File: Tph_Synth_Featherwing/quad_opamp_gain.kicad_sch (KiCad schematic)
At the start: 26 parts, among them U3 Opamp_Quad_Generic

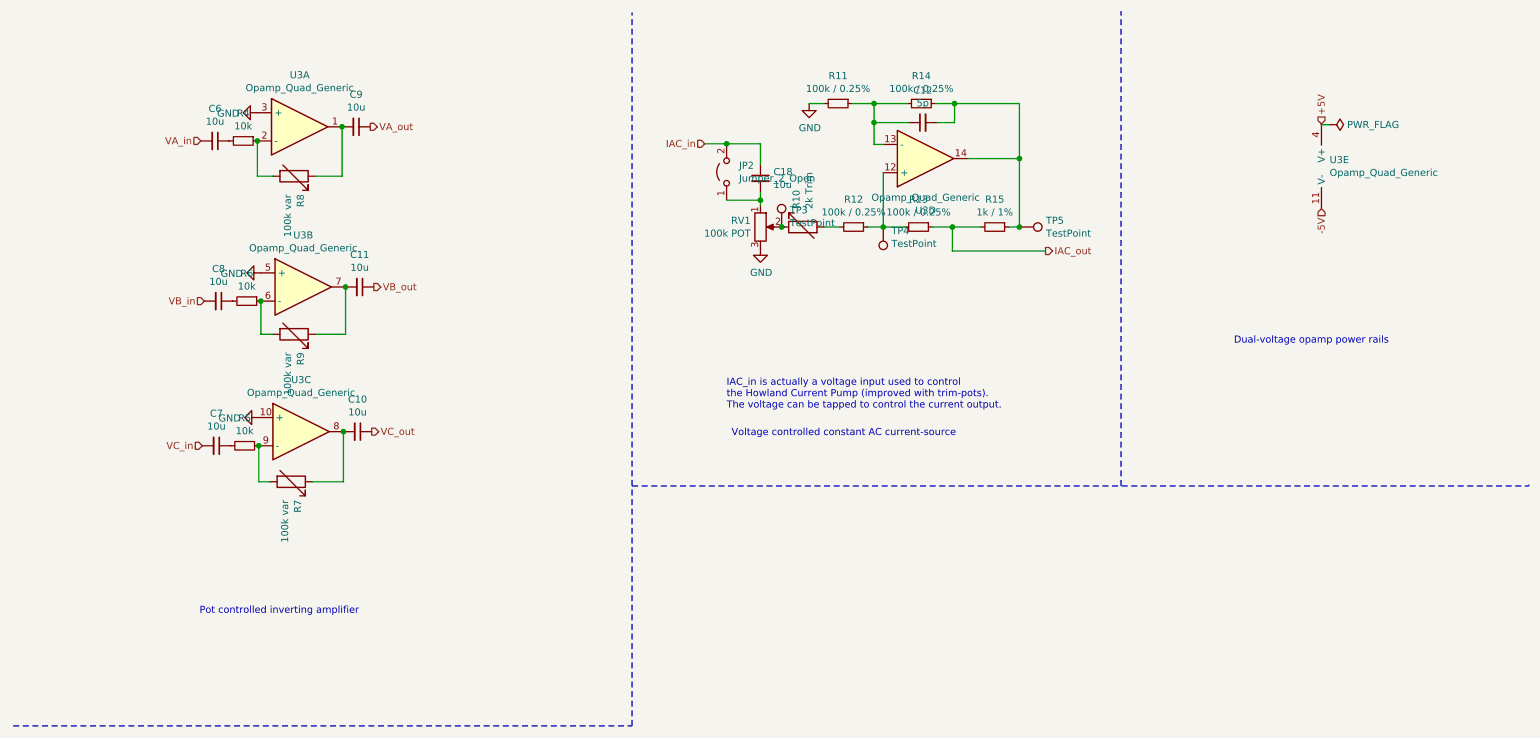
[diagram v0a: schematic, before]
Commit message: Upgrade design to KiCad 10; clear ERC and DRC violations
Co-authored-by: Copilot <223556219+Copilot@users.noreply.github.com>
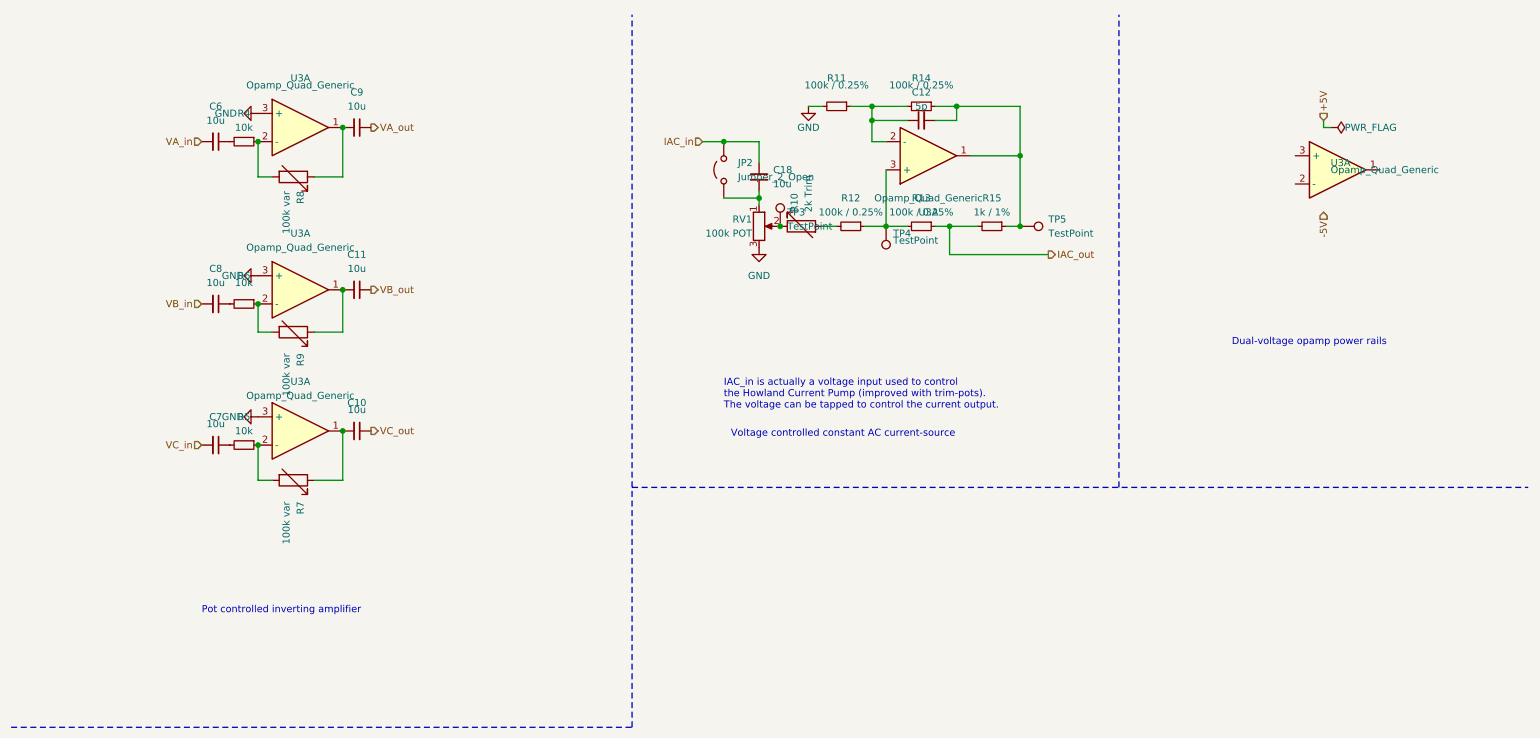
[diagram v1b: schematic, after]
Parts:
- RV1: symbol Device:R_POT -> Device:R_Potentiometer
- U3: symbol Device:Opamp_Quad_Generic -> Device:Opamp_Quad
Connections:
- net +5V: no longer U3.4 (V+)
- net -5V: no longer U3.11 (V-)
- net GND: now also U3.3 (+), U3.3 (+); no longer U3.10 (+), U3.5 (+)
- net at R6.1, R9.2: now also U3.2 (-); no longer U3.6 (-)
- net at C11.2, R9.1: now also U3.1; no longer U3.7
- net at C10.2, R7.1: now also U3.1; no longer U3.8
- net at R5.1, R7.2: now also U3.2 (-); no longer U3.9 (-)
- net at R12.1, R13.2, TP4.1: now also U3.3 (+); no longer U3.12 (+)
- net at C12.1, R11.1, R14.2: now also U3.2 (-); no longer U3.13 (-)
- net at C12.2, R14.1, R15.1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: now also U3.1; no longer U3.14
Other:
- moved on the sheet: C11, C8, R11, R12, R13, R14, R15, R6, TP4, U3A

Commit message: Release v0.4 with complete KiCad 10 schematic-PCB parity
Synchronize pad nets, schematic paths, component fields and BOM exclusions while retaining routing and placement. Restore project-local STEP models, fix edge silkscreen using local footprint variants, update revision metadata and improve schematic readability. Include inspected PDF and PCB renders.

Co-authored-by: Copilot <223556219+Copilot@users.noreply.github.com>
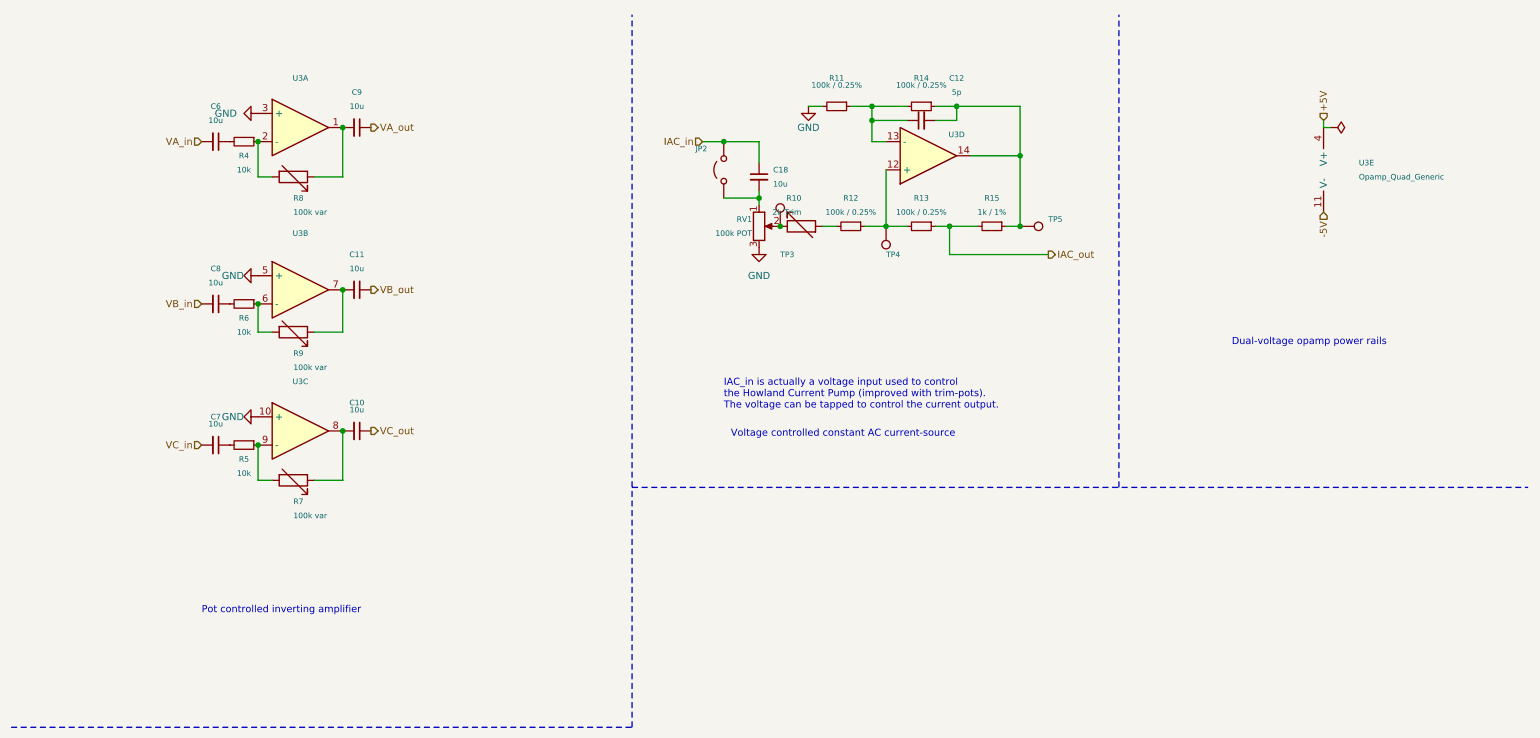
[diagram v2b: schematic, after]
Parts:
- JP2, TP3, TP4, TP5: now left out of the parts list
- R7, R8, R9, RV1: footprint Potentiometer_THT:Potentiometer_Bourns_PTV09A-2_Single_Horizontal -> FeatherWing_v04:Potentiometer_Bourns_PTV09A-2_Single_Horizontal_EdgeMounted
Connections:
- net +5V: now also U3.4 (V+)
- net -5V: now also U3.11 (V-)
- net GND: now also U3.10 (+), U3.5 (+); no longer U3.3 (+), U3.3 (+)
- net at C11.2, R9.1: now also U3.7; no longer U3.1
- net at R6.1, R9.2: now also U3.6 (-); no longer U3.2 (-)
- net at C10.2, R7.1: now also U3.8; no longer U3.1
- net at R5.1, R7.2: now also U3.9 (-); no longer U3.2 (-)
- net at C12.2, R14.1, R15.1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: now also U3.14; no longer U3.1
- net at C12.1, R11.1, R14.2: now also U3.13 (-); no longer U3.2 (-)
- net at R12.1, R13.2, TP4.1: now also U3.12 (+); no longer U3.3 (+)
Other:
- title: (none) -> 3-Phase Synth FeatherWing
